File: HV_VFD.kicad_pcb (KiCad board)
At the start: 2 copper layers, 197 x 77.5 mm, 3 parts, among them Q1 SEMiX402GB066HDs, Q2 SEMiX402GB066HDs, Q3 SEMiX402GB066HDs

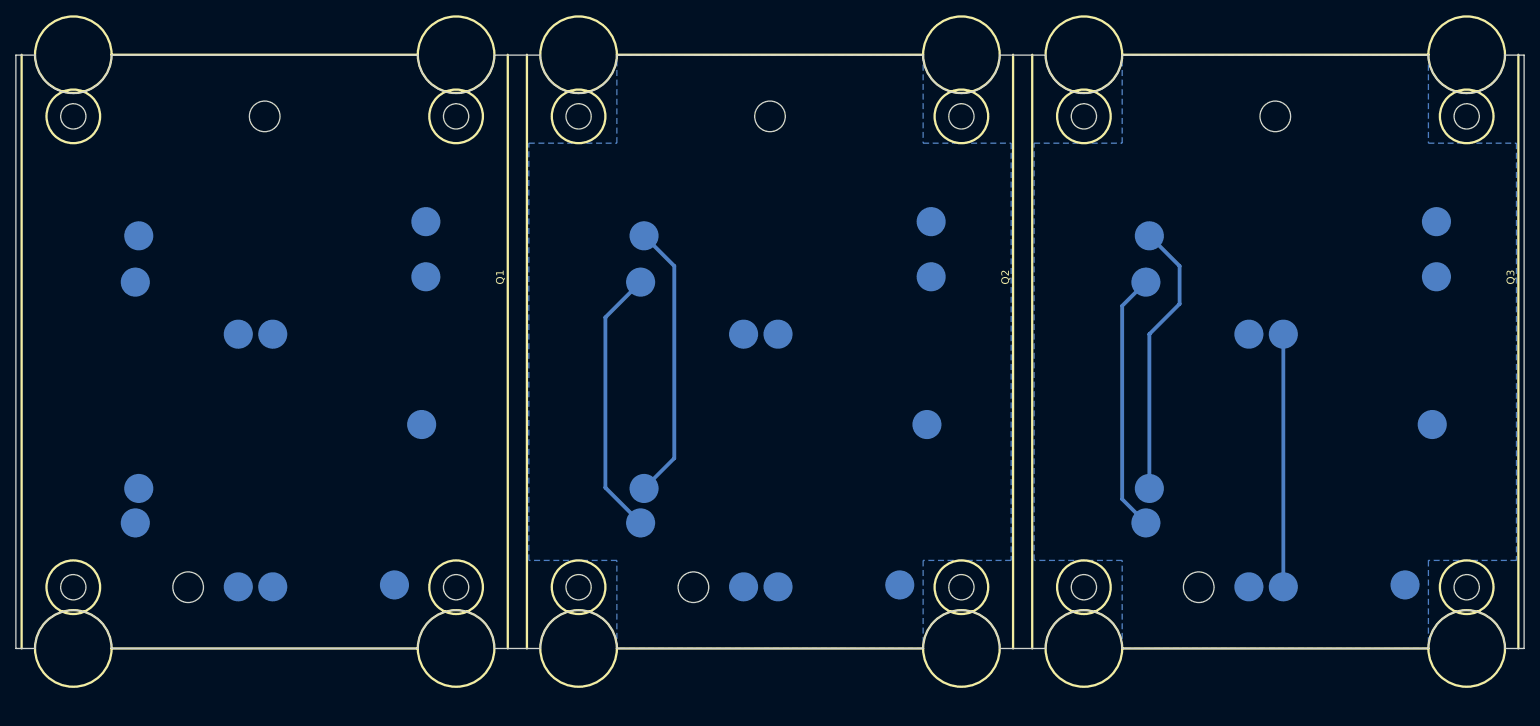
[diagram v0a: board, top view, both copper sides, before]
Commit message: added basic bootstrap and desat diodes
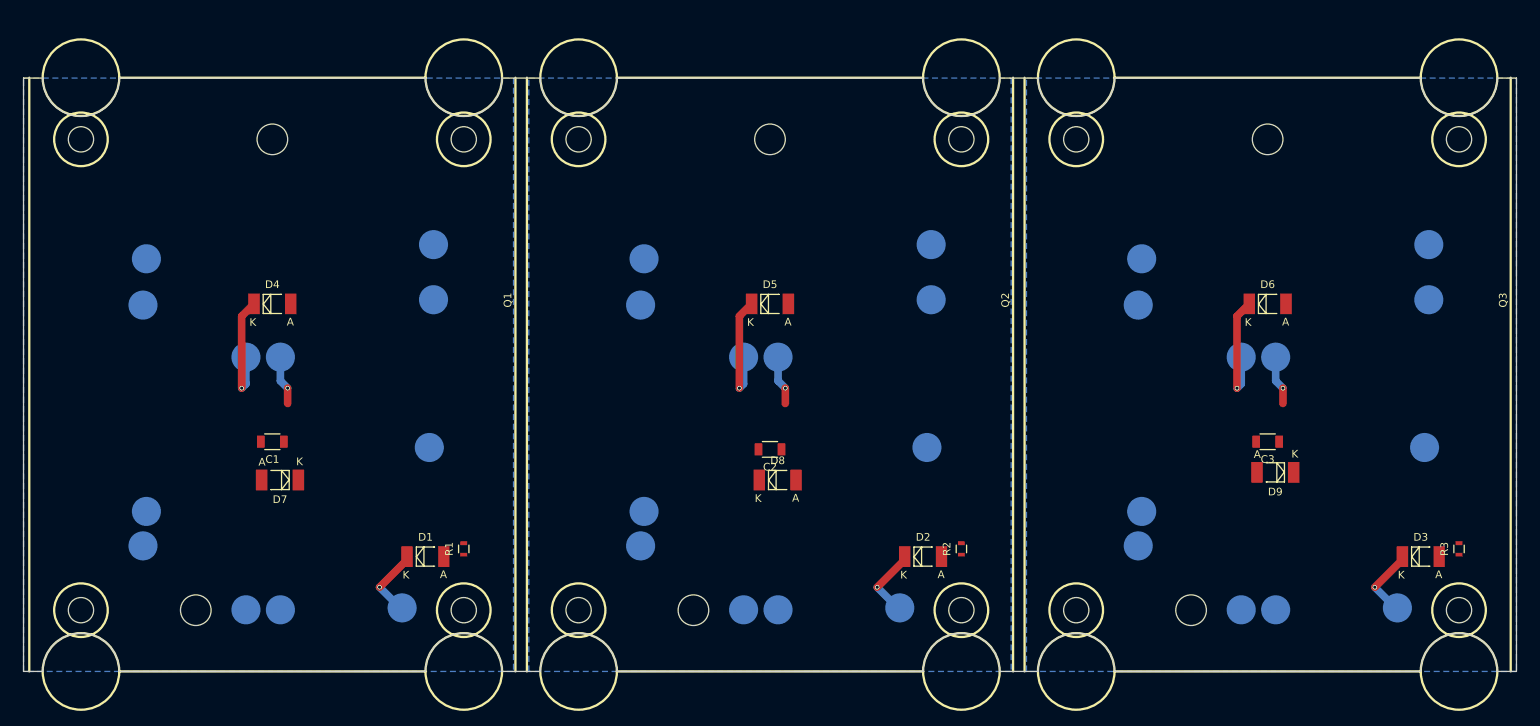
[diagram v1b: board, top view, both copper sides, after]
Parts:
- added C1: C, Capacitors_SMD:C_1206, F.Cu at (90.0, 103.0)
- added C2: C, Capacitors_SMD:C_1206, F.Cu at (155.0, 104.0)
- added C3: C, Capacitors_SMD:C_1206, F.Cu at (220.0, 103.0)
- added D1: D, Diodes_SMD:MELF_Standard, F.Cu at (110.0, 118.0)
- added D2: D, Diodes_SMD:MELF_Standard, F.Cu at (175.0, 118.0)
- added D3: D, Diodes_SMD:MELF_Standard, F.Cu at (240.0, 118.0)
- added D4: D, Diodes_SMD:MELF_Standard, F.Cu at (90.0, 85.0)
- added D5: D, Diodes_SMD:MELF_Standard, F.Cu at (155.0, 85.0)
- added D6: D, Diodes_SMD:MELF_Standard, F.Cu at (220.0, 85.0)
- added D7: D, Diodes_SMD:MELF_Standard, F.Cu at (91.0, 108.0)
- added D8: D, Diodes_SMD:MELF_Standard, F.Cu at (156.0, 108.0)
- added D9: D, Diodes_SMD:MELF_Standard, F.Cu at (221.0, 107.0)
- added R1: R, Resistors_SMD:R_0603, F.Cu at (115.0, 117.0)
- added R2: R, Resistors_SMD:R_0603, F.Cu at (180.0, 117.0)
- added R3: R, Resistors_SMD:R_0603, F.Cu at (245.0, 117.0)
- moved Q1 3.16 mm to (80.0, 125.0)
- moved Q3 3.16 mm to (210.0, 125.0)
- moved Q2 3.00 mm to (145.0, 125.0)
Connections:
- net Net-(Q1-Pad10) renamed Q1L_G
- net Net-(Q1-Pad12) renamed Q1H_G
- net Net-(Q1-Pad5) renamed Q1L_EM
- net Net-(Q2-Pad10) renamed Q2L_G
- net Net-(Q2-Pad12) renamed Q2H_G
- net Net-(Q2-Pad5) renamed Q2L_EM
- net Net-(Q3-Pad10) renamed Q3L_G
- net Net-(Q3-Pad12) renamed Q3H_G
- net Net-(Q3-Pad5) renamed Q3L_EM
- Q1 pad 11: Net-(Q1-Pad11) -> Q1H_EM
- Q2 pad 11: Net-(Q2-Pad11) -> Q2H_EM
- Q3 pad 11: Net-(Q3-Pad11) -> Q3H_EM
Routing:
- net Q2L_G: track 36.3 -> 0.00 mm
- net Q3L_G: track 36.3 -> 0.00 mm
- net Q2L_EM: track 35.3 -> 0.00 mm
- net Q3L_EM: track 34.0 -> 0.00 mm
- net Q3H_G: track 33.0 -> 6.44 mm, vias 0 -> 1
- net Q3H_EM: track 0.00 -> 15.9 mm, vias 0 -> 1
- net Q2H_EM: track 0.00 -> 15.9 mm, vias 0 -> 1
- net Q1H_EM: track 0.00 -> 15.9 mm, vias 0 -> 1
- net Net-(D3-Pad1): track 0.00 -> 9.56 mm, vias 0 -> 1
- net Net-(D2-Pad1): track 0.00 -> 9.56 mm, vias 0 -> 1
- net Net-(D1-Pad1): track 0.00 -> 9.56 mm, vias 0 -> 1
- net Q1H_G: track 0.00 -> 6.44 mm, vias 0 -> 1
- net Q2H_G: track 0.00 -> 6.44 mm, vias 0 -> 1
- added copper zone on B.Cu, net Net-(Q1-Pad14)
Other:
- board size 197 x 77.5 mm -> 195 x 77.5 mm

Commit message: added gate drivers, increased FET spacing
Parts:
- removed C1, C2, C3: C, Capacitors_SMD:C_1206
- removed D1, D2, D3, D4, D5, D6, D7, D8, D9: D, Diodes_SMD:MELF_Standard
- removed Q1, Q2, Q3: SEMiX402GB066HDs, VFD_parts:SEMiX_2s
- removed R1, R2, R3: R, Resistors_SMD:R_0603
- added C301: C, Capacitors_SMD:C_1206, F.Cu at (59.0, 72.0)
- added C302: C, Capacitors_SMD:C_1206, F.Cu at (50.0, 71.0)
- added C303: C, Capacitors_SMD:C_1206, F.Cu at (158.0, 72.5)
- added C304: C, Capacitors_SMD:C_1206, F.Cu at (141.0, 72.0)
- added C305: C, Capacitors_SMD:C_1206, F.Cu at (235.5, 74.0)
- added C306: C, Capacitors_SMD:C_1206, F.Cu at (242.5, 74.0)
- added D201: D, Diodes_SMD:MELF_Standard, F.Cu at (71.5, 117.0)
- added D202: D, Diodes_SMD:MELF_Standard, F.Cu at (167.0, 117.5)
- added D203: D, Diodes_SMD:MELF_Standard, F.Cu at (261.5, 115.5)
- added D204: D, Diodes_SMD:MELF_Standard, F.Cu at (50.5, 99.5)
- added D205: D, Diodes_SMD:MELF_Standard, F.Cu at (145.5, 101.5)
- added D206: D, Diodes_SMD:MELF_Standard, F.Cu at (240.5, 100.0)
- added D207: D, Diodes_SMD:DO-214AB, F.Cu at (29.5, 88.5)
- added D208: D, Diodes_SMD:DO-214AB, F.Cu at (124.5, 88.5)
- added D209: D, Diodes_SMD:DO-214AB, F.Cu at (218.0, 88.5)
- added D210: D, Diodes_SMD:DO-214AB, F.Cu at (29.5, 113.0)
- added D211: D, Diodes_SMD:DO-214AB, F.Cu at (123.5, 113.0)
- added D212: D, Diodes_SMD:DO-214AB, F.Cu at (219.0, 113.0)
- added D301: D, Diodes_SMD:MELF_Standard, F.Cu at (58.0, 76.5)
- added D302: D, Diodes_SMD:MELF_Standard, F.Cu at (147.5, 70.0)
- added D303: D, Diodes_SMD:MELF_Standard, F.Cu at (257.0, 69.5)
- added Q201: SEMiX402GB066HDs, VFD_parts:SEMiX_2s_7nc, F.Cu at (45.0, 125.0)
- added Q202: SEMiX402GB066HDs, VFD_parts:SEMiX_2s_7nc, F.Cu at (140.0, 125.0)
- added Q203: SEMiX402GB066HDs, VFD_parts:SEMiX_2s_7nc, F.Cu at (235.0, 125.0)
- added R201: RGh, Resistors_SMD:R_1812, F.Cu at (56.5, 99.5)
- added R202: RGh, Resistors_SMD:R_1812, F.Cu at (151.0, 101.5)
- added R203: RGh, Resistors_SMD:R_1812, F.Cu at (246.5, 100.0)
- added R204: RGh, Resistors_SMD:R_1812, F.Cu at (56.5, 116.0)
- added R205: RGh, Resistors_SMD:R_1812, F.Cu at (151.0, 116.0)
- added R206: RGh, Resistors_SMD:R_1812, F.Cu at (245.5, 117.0)
- added R207: RGl, Resistors_SMD:R_1812, F.Cu at (38.5, 104.5)
- added R208: RGl, Resistors_SMD:R_1812, F.Cu at (133.5, 103.0)
- added R209: RGl, Resistors_SMD:R_1812, F.Cu at (236.0, 110.5)
- added R210: RGl, Resistors_SMD:R_1812, F.Cu at (30.0, 76.5)
- added R211: RGl, Resistors_SMD:R_1812, F.Cu at (125.5, 76.0)
- added R212: RGl, Resistors_SMD:R_1812, F.Cu at (220.0, 76.5)
- added R213: REl, Resistors_SMD:R_1812, F.Cu at (37.5, 93.0)
- added R214: REl, Resistors_SMD:R_1812, F.Cu at (132.5, 93.0)
- added R215: REl, Resistors_SMD:R_1812, F.Cu at (228.5, 93.0)
- added R216: REl, Resistors_SMD:R_1812, F.Cu at (47.0, 117.0)
- added R217: REl, Resistors_SMD:R_1812, F.Cu at (141.5, 117.0)
- added R218: REl, Resistors_SMD:R_1812, F.Cu at (236.5, 116.0)
- added R301: R, Resistors_SMD:R_0603, F.Cu at (45.5, 72.5)
- added R302: R, Resistors_SMD:R_0603, F.Cu at (152.5, 75.0)
- added R303: R, Resistors_SMD:R_0603, F.Cu at (257.5, 75.0)
- added R304: R, Resistors_SMD:R_1812, F.Cu at (63.0, 152.0)
- added R305: R, Resistors_SMD:R_1812, F.Cu at (127.5, 155.0)
- added R306: R, Resistors_SMD:R_1812, F.Cu at (202.5, 140.0)
- added R307: R, Resistors_SMD:R_1812, F.Cu at (33.5, 148.5)
- added R308: R, Resistors_SMD:R_1812, F.Cu at (145.0, 150.0)
- added R309: R, Resistors_SMD:R_1812, F.Cu at (251.0, 140.5)
- added R310: R, Resistors_SMD:R_0603, F.Cu at (49.0, 148.0)
- added R311: R, Resistors_SMD:R_0603, F.Cu at (158.0, 151.5)
- added R312: R, Resistors_SMD:R_0603, F.Cu at (266.0, 144.5)
- added U301: 1EDI60H12AH, VFD_parts:PG-DSO-8-59, F.Cu at (64.5, 163.0)
- added U302: 1EDI60H12AH, VFD_parts:PG-DSO-8-59, F.Cu at (128.5, 165.0)
- added U303: 1EDI60H12AH, VFD_parts:PG-DSO-8-59, F.Cu at (203.0, 153.0)
- added U304: 1EDI60H12AH, VFD_parts:PG-DSO-8-59, F.Cu at (33.0, 159.5)
- added U305: 1EDI60H12AH, VFD_parts:PG-DSO-8-59, F.Cu at (148.0, 161.0)
- added U306: 1EDI60H12AH, VFD_parts:PG-DSO-8-59, F.Cu at (251.5, 150.0)
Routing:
- net Q3H_EM: track 15.9 -> 0.00 mm, vias 1 -> 0
- net Q2H_EM: track 15.9 -> 0.00 mm, vias 1 -> 0
- net Q1H_EM: track 15.9 -> 0.00 mm, vias 1 -> 0
- net Net-(D3-Pad1): track 9.56 -> 0.00 mm, vias 1 -> 0
- net Net-(D2-Pad1): track 9.56 -> 0.00 mm, vias 1 -> 0
- net Net-(D1-Pad1): track 9.56 -> 0.00 mm, vias 1 -> 0
- net Q1H_G: track 6.44 -> 0.00 mm, vias 1 -> 0
- net Q3H_G: track 6.44 -> 0.00 mm, vias 1 -> 0
- net Q2H_G: track 6.44 -> 0.00 mm, vias 1 -> 0
- added copper zone on B.Cu, net Net-(Q201-Pad14)
- added copper zone on B.Cu, net Net-(Q202-Pad14)
- added copper zone on B.Cu, net Net-(Q203-Pad14)
- removed copper zone on B.Cu, net Net-(Q1-Pad14)
- removed copper zone on B.Cu, net Net-(Q2-Pad14)
- removed copper zone on B.Cu, net Net-(Q3-Pad14)
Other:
- board size 195 x 77.5 mm -> 253 x 77.5 mm
